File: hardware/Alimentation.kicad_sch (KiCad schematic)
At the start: 10 parts, among them U4 AP2112R5-3.3TRG1

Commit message: Assignation terminee
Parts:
- C7, C8: footprint (none) -> Capacitor_SMD:C_0805_2012Metric
- D4: value LED -> VBUS_LED; footprint (none) -> LED_SMD:LED_0805_2012Metric
- D5: value LED -> 3v3_LED; footprint (none) -> LED_SMD:LED_0805_2012Metric
- R28, R29: footprint (none) -> Resistor_SMD:R_0805_2012Metric
- TP11, TP12, TP13: footprint (none) -> TestPoint:TestPoint_Loop_D2.50mm_Drill1.0mm
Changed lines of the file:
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@@
 			)
 		)
-		(property "Value" "LED"
+		(property "Value" "3v3_LED"
 			(at 194.31 105.7274 90)
 			(show_name no)
@@
 			)
 		)
-		(property "Footprint" ""
+		(property "Footprint" "LED_SMD:LED_0805_2012Metric"
 			(at 190.5 102.87 0)
 			(hide yes)
@@
 			)
 		)
-		(property "Footprint" ""
+		(property "Footprint" "TestPoint:TestPoint_Loop_D2.50mm_Drill1.0mm"
 			(at 195.58 82.55 0)
 			(hide yes)
@@
 			)
 		)
-		(property "Footprint" ""
+		(property "Footprint" "Capacitor_SMD:C_0805_2012Metric"
 			(at 126.6952 97.79 0)
 			(hide yes)
@@
 			)
 		)
-		(property "Footprint" ""
+		(property "Footprint" "TestPoint:TestPoint_Loop_D2.50mm_Drill1.0mm"
 			(at 120.65 82.55 0)
 			(hide yes)
@@
 			)
 		)
-		(property "Footprint" ""
+		(property "Footprint" "Resistor_SMD:R_0805_2012Metric"
 			(at 113.792 92.71 90)
 			(hide yes)
@@
 			)
 		)
-		(property "Footprint" ""
+		(property "Footprint" "TestPoint:TestPoint_Loop_D2.50mm_Drill1.0mm"
 			(at 228.6 110.49 0)
 			(hide yes)
@@
 			)
 		)
-		(property "Footprint" ""
+		(property "Footprint" "Resistor_SMD:R_0805_2012Metric"
 			(at 188.722 92.71 90)
 			(hide yes)
@@
 			)
 		)
-		(property "Value" "LED"
+		(property "Value" "VBUS_LED"
 			(at 119.38 105.7274 90)
 			(show_name no)
@@
 			)
 		)
-		(property "Footprint" ""
+		(property "Footprint" "LED_SMD:LED_0805_2012Metric"
 			(at 115.57 102.87 0)
 			(hide yes)
@@
 			)
 		)
-		(property "Footprint" ""
+		(property "Footprint" "Capacitor_SMD:C_0805_2012Metric"
 			(at 177.4952 95.25 0)
 			(hide yes)

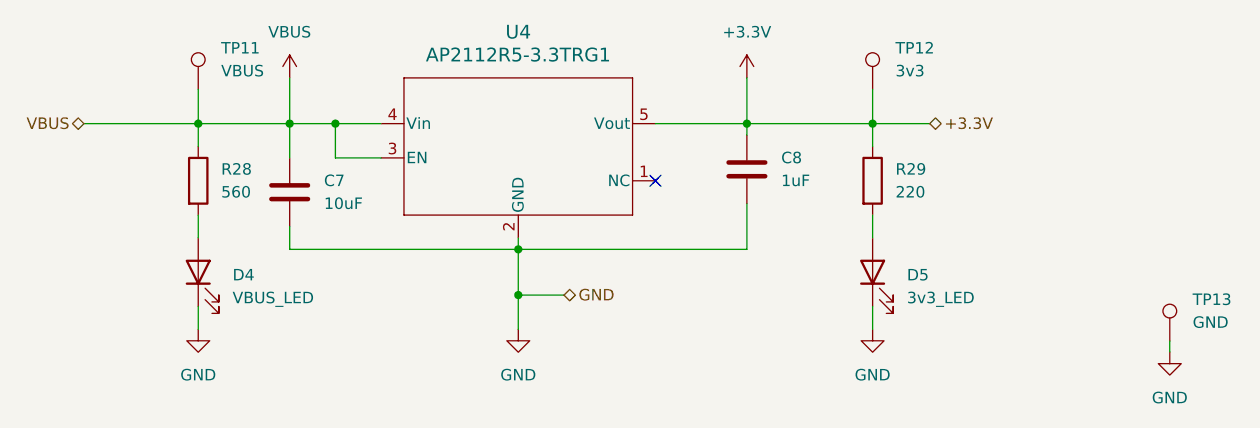
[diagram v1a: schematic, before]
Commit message: USB connector CC Resistor not mount text added
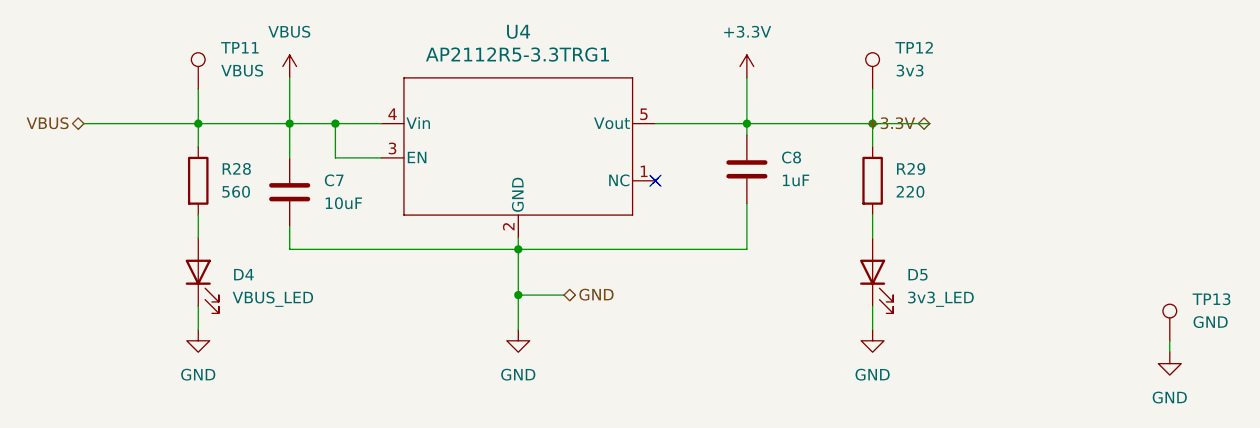
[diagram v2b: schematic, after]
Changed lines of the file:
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@@
 	(hierarchical_label "+3.3V"
 		(shape bidirectional)
-		(at 196.85 86.36 0)
+		(at 196.85 86.36 180)
 		(effects
 			(font
 				(size 1.27 1.27)
 			)
-			(justify left)
+			(justify right)
 		)
 	)
